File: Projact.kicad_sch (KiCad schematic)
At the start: 22 parts, among them J1 Conn_01x01, J2 Conn_01x01, J3 Conn_01x01, J4 Conn_01x01, P1 USB_C_Plug_USB2.0, P2 USB_C_Plug_USB2.0, U1 TP4056, U2 DW01, U3 FS8205A

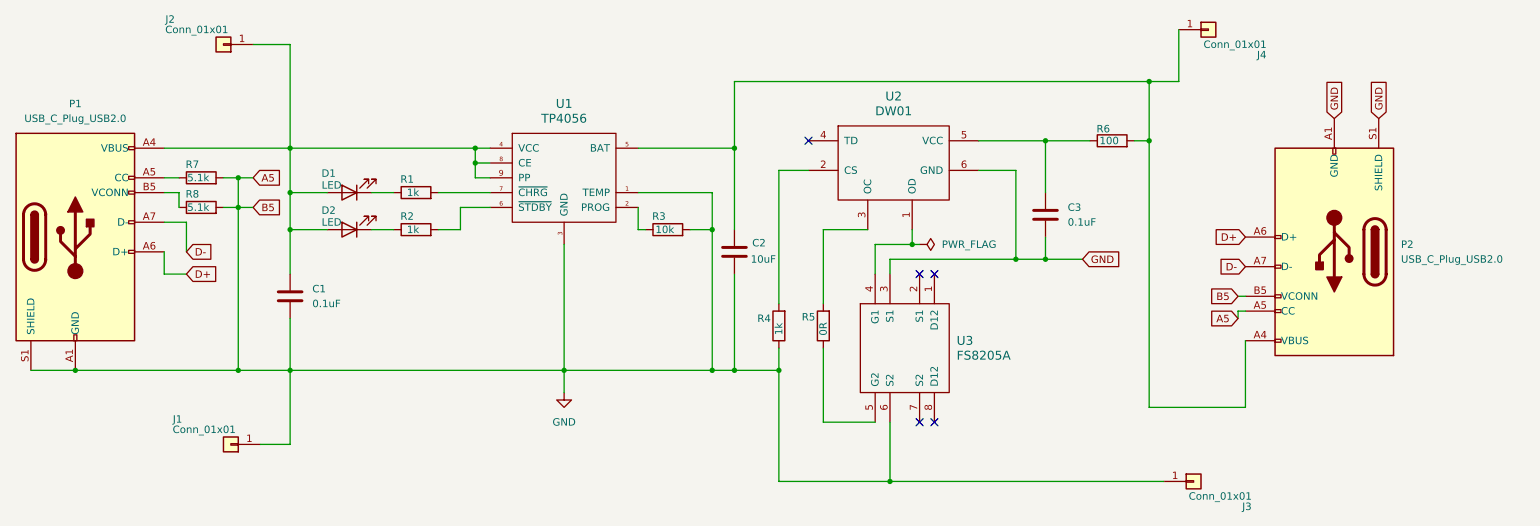
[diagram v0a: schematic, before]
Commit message: fix cc pin pull down
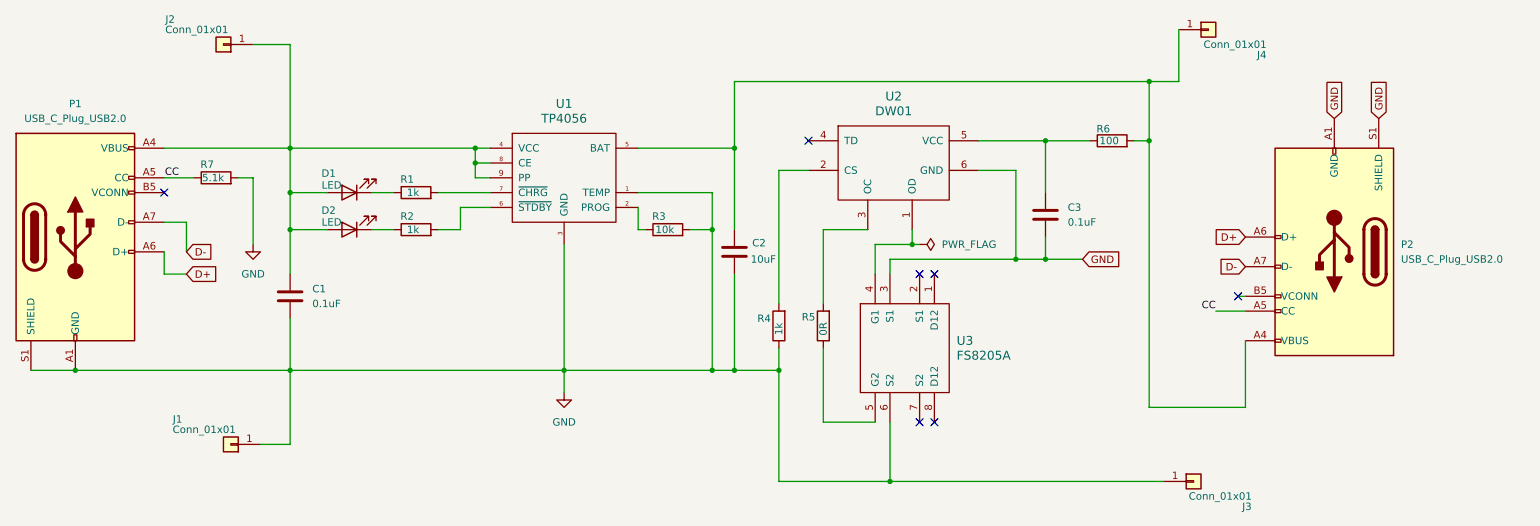
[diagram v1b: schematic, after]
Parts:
- removed R8: 5.1k, symbol Device:R
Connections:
- net GND: no longer P2.A5 (CC), P2.B5 (VCONN)
- net CC: now reaches P1.A5 (CC), R7.1
- net CC: now also P2.A5 (CC)
- no-connect marks 5 -> 7
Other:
- moved on the sheet: R7
